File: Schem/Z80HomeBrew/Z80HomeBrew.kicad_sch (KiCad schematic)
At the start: 0 parts

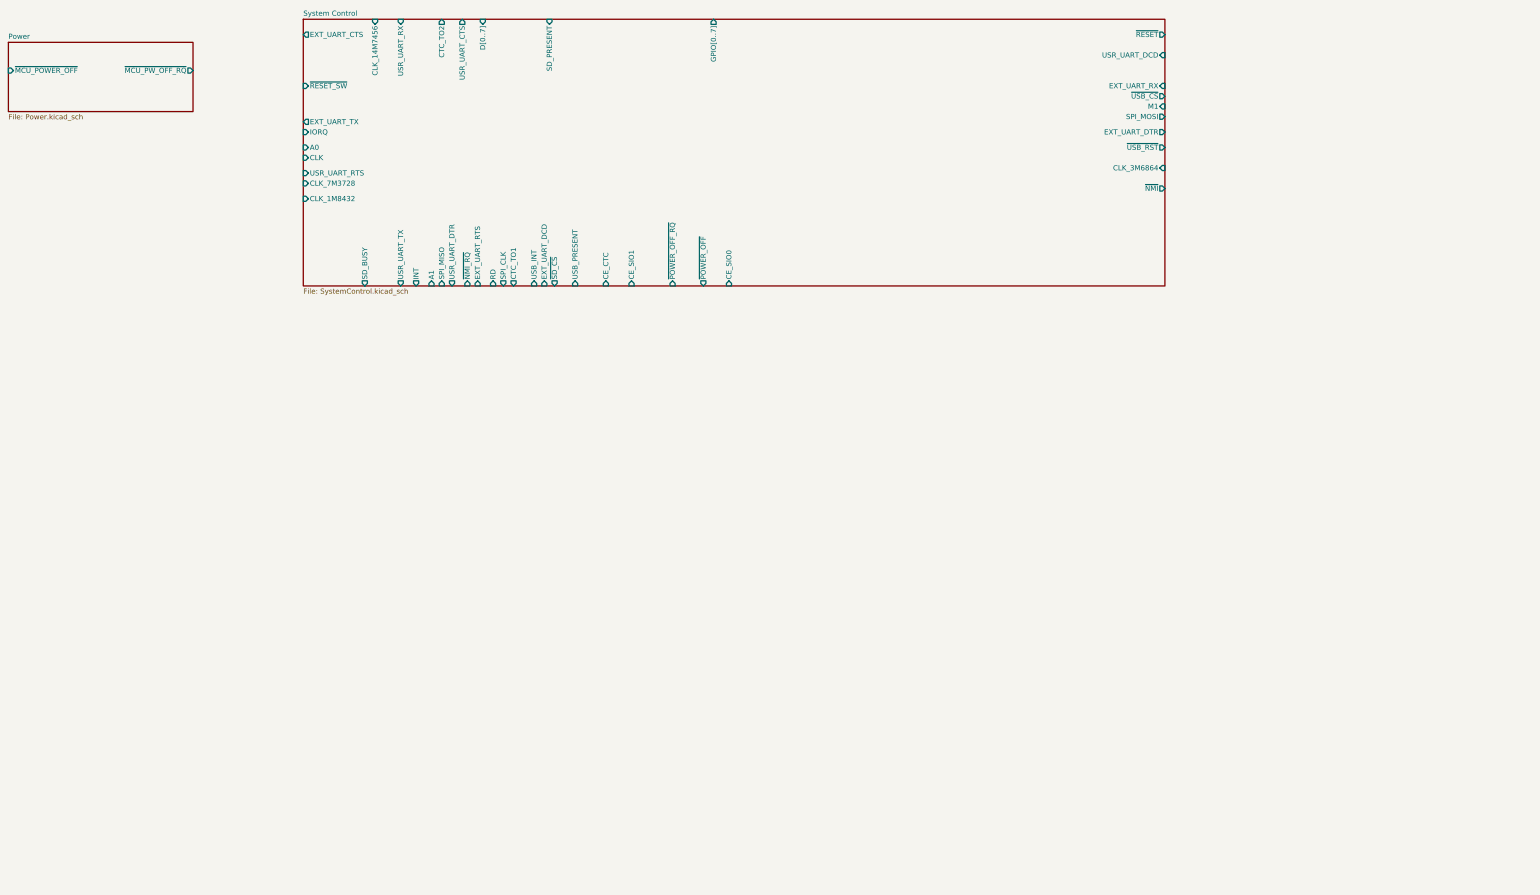
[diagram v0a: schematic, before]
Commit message: Added CPU, Address Decoding, Clock Tree, Console Port, SD Card, USB Ports schematics and associated symbols and footprints.
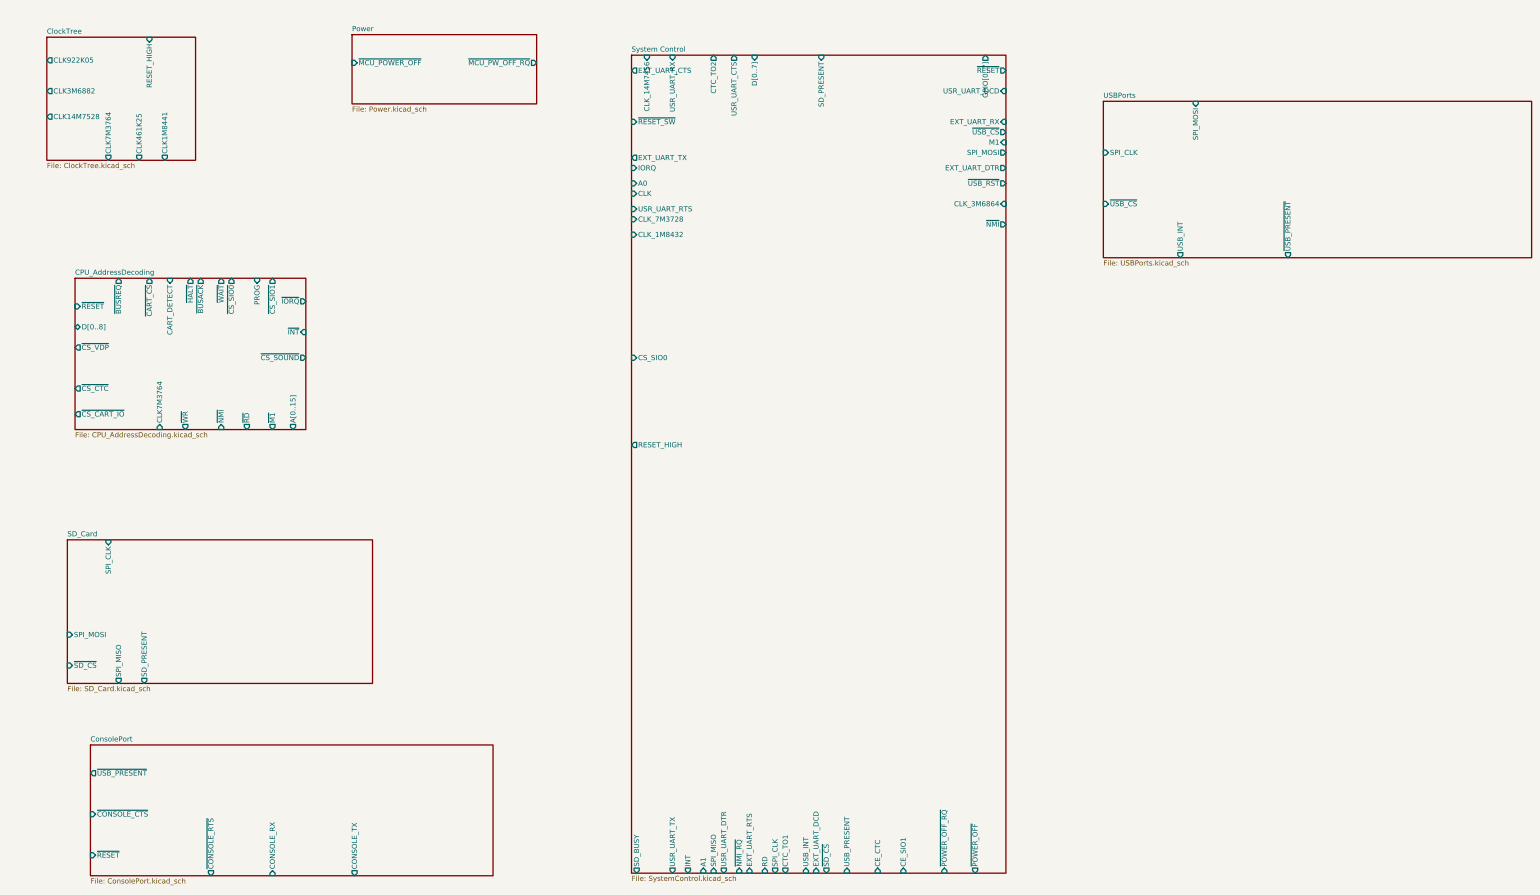
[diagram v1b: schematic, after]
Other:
- added sheet CPU_AddressDecoding (CPU_AddressDecoding.kicad_sch)
- added sheet ClockTree (ClockTree.kicad_sch)
- added sheet ConsolePort (ConsolePort.kicad_sch)
- added sheet SD_Card (SD_Card.kicad_sch)
- added sheet USBPorts (USBPorts.kicad_sch)
- sheet System Control ports: added CS_SIO0, RESET_HIGH; removed CE_SIO0
